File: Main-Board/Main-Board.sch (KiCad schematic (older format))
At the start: 24 parts, among them J1 Power_In, J2 ESC_1, J3 ESC_2, J4 ESC_3, J5 ESC_4, J8 Receiver, J9 Aux, U1 MCP6001U

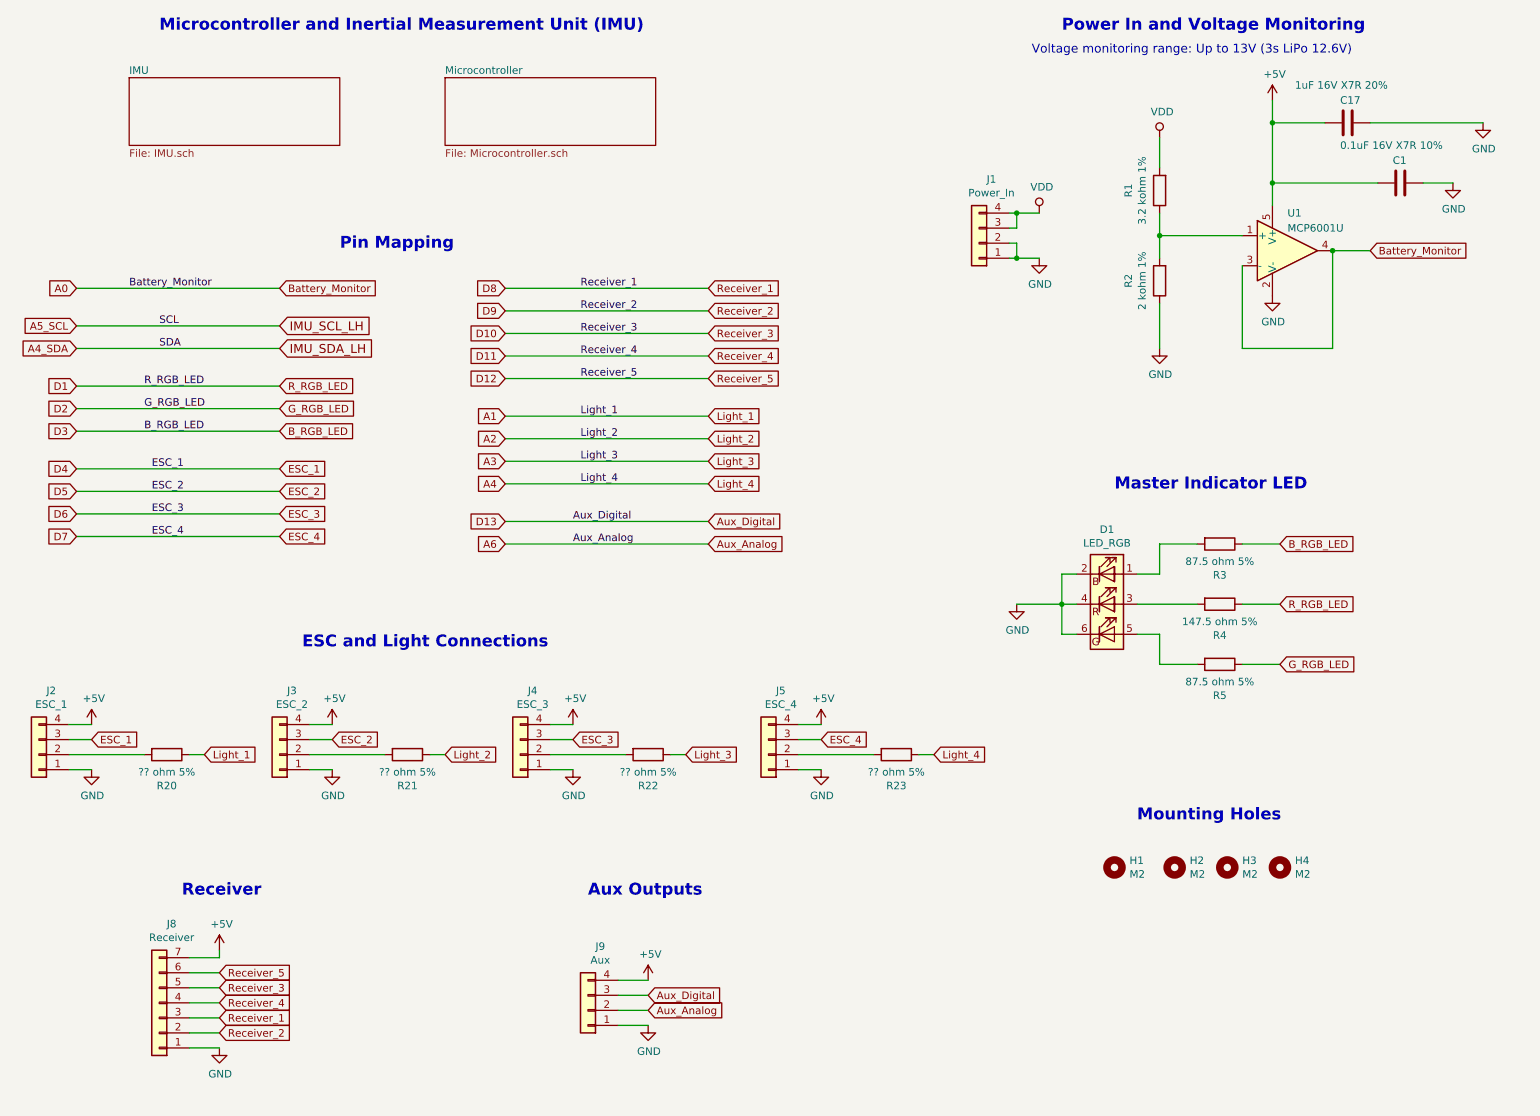
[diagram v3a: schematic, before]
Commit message: Review IMU, changed power in connector to 6 pos to prevent mis mating
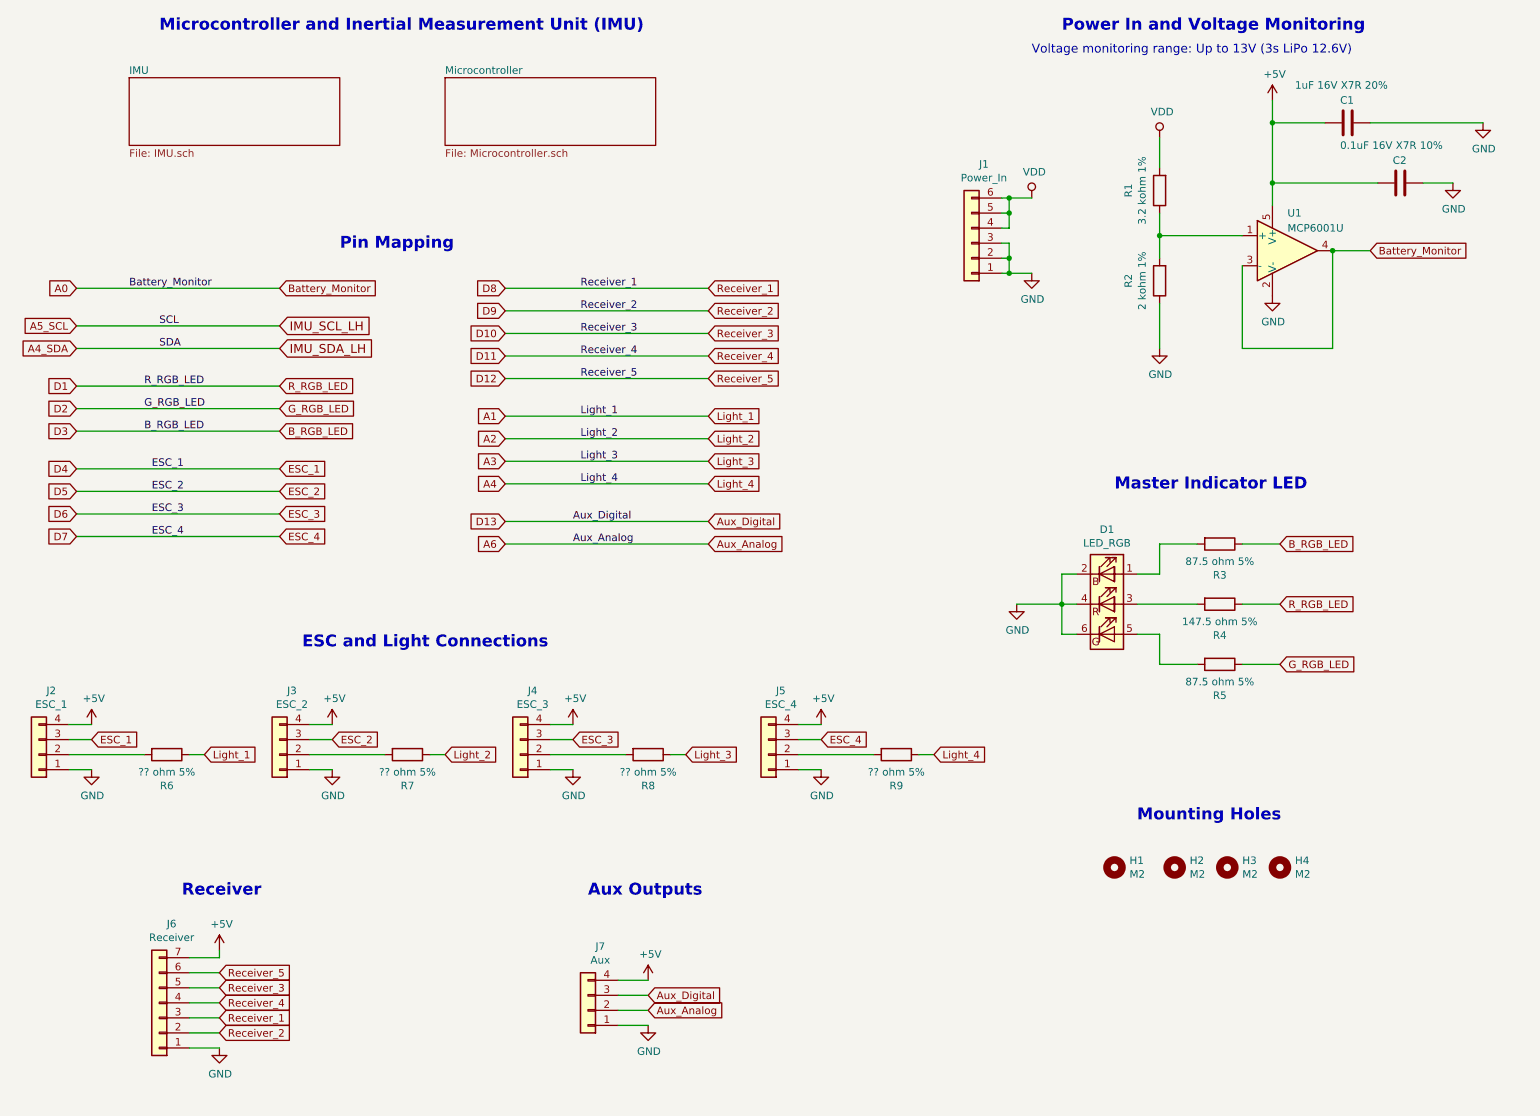
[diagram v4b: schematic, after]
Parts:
- removed J1: Power_In, Connector_JST:JST_GH_BM04B-GHS-TBT_1x04-1MP_P1.25mm_Vertical, symbol Connector_Generic:Conn_01x04
- added J1: Power_In, Connector_JST:JST_GH_BM06B-GHS-TBT_1x06-1MP_P1.25mm_Vertical, symbol Connector_Generic:Conn_01x06
- renumbered C17 to C1, C1 to C2, J8 to J6, J9 to J7, R20 to R6, R21 to R7, R22 to R8, R23 to R9
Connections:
- net GND: now also J1.1 (Pin_1), J1.2 (Pin_2), J1.3 (Pin_3)
- net VDD: now also J1.4 (Pin_4), J1.5 (Pin_5), J1.6 (Pin_6)

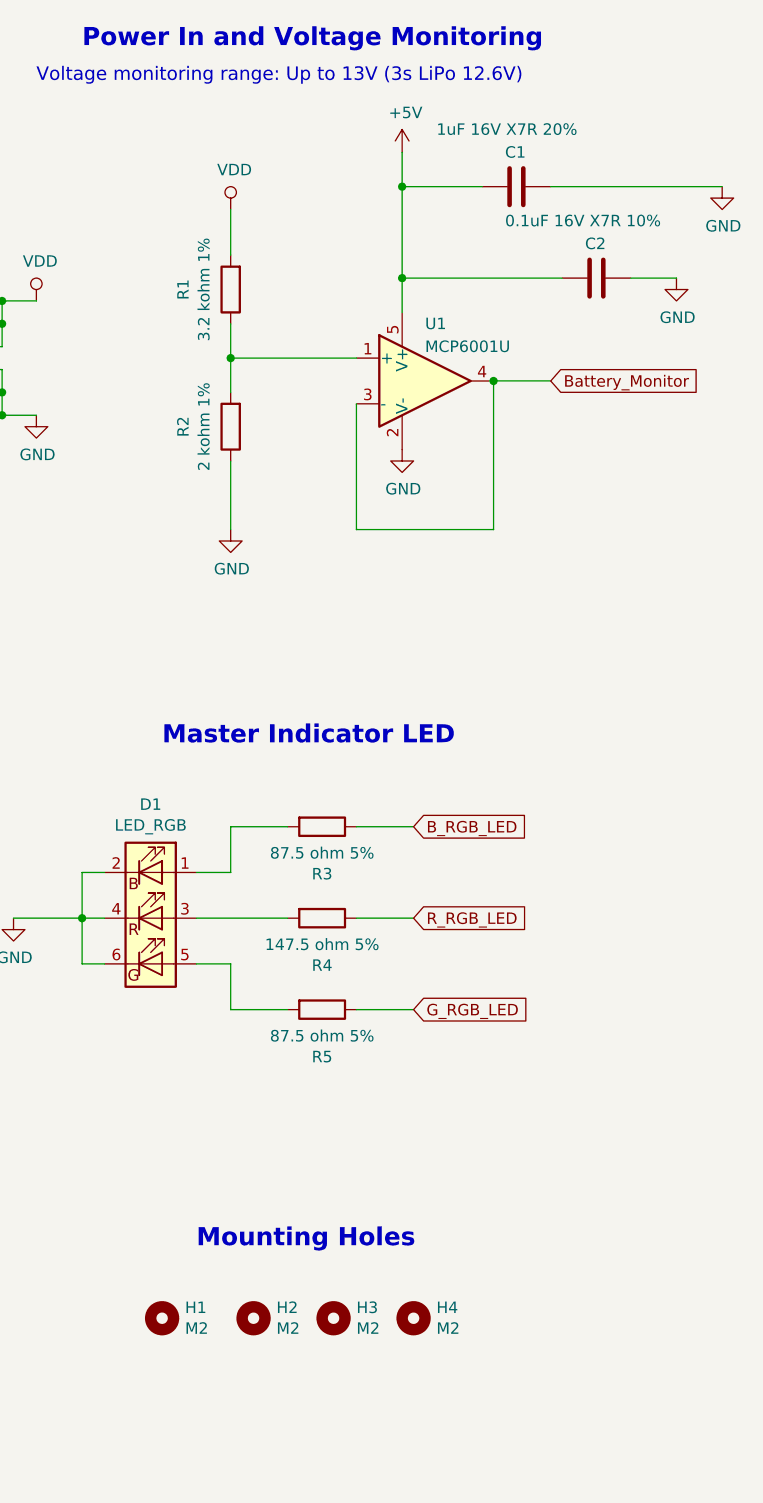
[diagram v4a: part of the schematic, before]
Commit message: Minor updates for components to reflect BOM
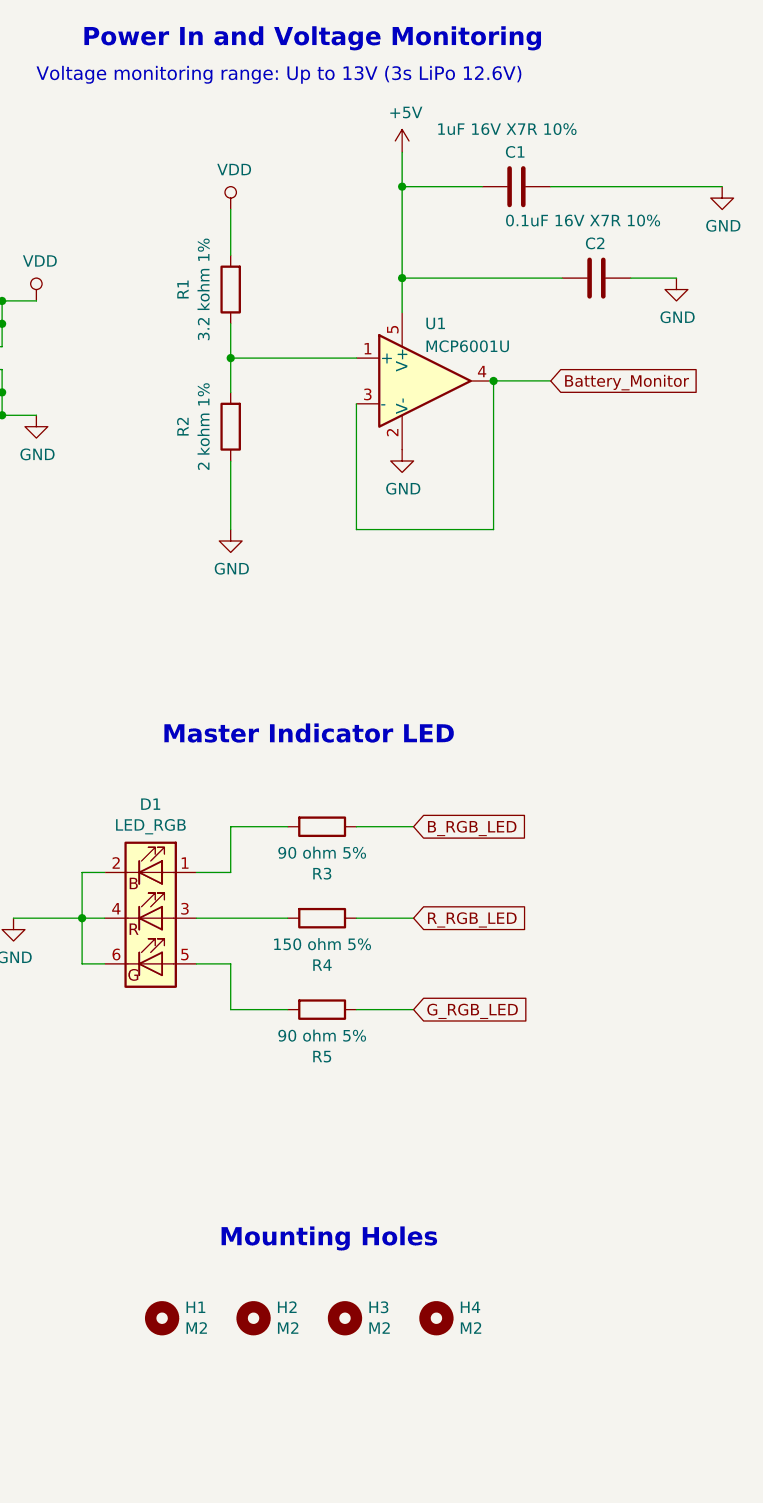
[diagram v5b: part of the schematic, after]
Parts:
- C1: value 1uF 16V X7R 20% -> 1uF 16V X7R 10%
- R3, R5: value 87.5 ohm 5% -> 90 ohm 5%
- R4: value 147.5 ohm 5% -> 150 ohm 5%
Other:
- moved on the sheet: H3, H4
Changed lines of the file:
@@
 encoding utf-8
 Sheet 1 3
-Title "Master Sheet"
-Date "2020-12-19"
+Title "Flight Controller"
+Date "2020-12-21"
 Rev "A"
 Comp ""
@@
 AR Path="/60061C0F" Ref="R3"  Part="1"
 F 0 "R3" V 8807 4150 50  0000 C CNN
-F 1 "87.5 ohm 5%" V 8716 4150 50  0000 C CNN
+F 1 "90 ohm 5%" V 8716 4150 50  0000 C CNN
 F 2 "Resistor_SMD:R_0603_1608Metric_Pad1.05x0.95mm_HandSolder" V 8530 4150 50  0001 C CNN
 F 3 "~" H 8600 4150 50  0001 C CNN
@@
 AR Path="/600625FC" Ref="R4"  Part="1"
 F 0 "R4" V 8807 4550 50  0000 C CNN
-F 1 "147.5 ohm 5%" V 8716 4550 50  0000 C CNN
+F 1 "150 ohm 5%" V 8716 4550 50  0000 C CNN
 F 2 "Resistor_SMD:R_0603_1608Metric_Pad1.05x0.95mm_HandSolder" V 8530 4550 50  0001 C CNN
 F 3 "~" H 8600 4550 50  0001 C CNN
@@
 AR Path="/60062A76" Ref="R5"  Part="1"
 F 0 "R5" V 8807 4950 50  0000 C CNN
-F 1 "87.5 ohm 5%" V 8716 4950 50  0000 C CNN
+F 1 "90 ohm 5%" V 8716 4950 50  0000 C CNN
 F 2 "Resistor_SMD:R_0603_1608Metric_Pad1.05x0.95mm_HandSolder" V 8530 4950 50  0001 C CNN
 F 3 "~" H 8600 4950 50  0001 C CNN
@@
 L Mechanical:MountingHole H3
 U 1 1 5FDEF850
-P 8650 6300
-F 0 "H3" H 8750 6346 50  0000 L CNN
-F 1 "M2" H 8750 6255 50  0000 L CNN
-F 2 "MountingHole:MountingHole_2.2mm_M2_ISO7380_Pad" H 8650 6300 50  0001 C CNN
-F 3 "~" H 8650 6300 50  0001 C CNN
-	1    8650 6300
+P 8700 6300
+F 0 "H3" H 8800 6346 50  0000 L CNN
+F 1 "M2" H 8800 6255 50  0000 L CNN
+F 2 "MountingHole:MountingHole_2.2mm_M2_ISO7380_Pad" H 8700 6300 50  0001 C CNN
+F 3 "~" H 8700 6300 50  0001 C CNN
+	1    8700 6300
 	1    0    0    -1
 $EndComp
@@
 L Mechanical:MountingHole H4
 U 1 1 5FDF1549
-P 9000 6300
-F 0 "H4" H 9100 6346 50  0000 L CNN
-F 1 "M2" H 9100 6255 50  0000 L CNN
-F 2 "MountingHole:MountingHole_2.2mm_M2_ISO7380_Pad" H 9000 6300 50  0001 C CNN
-F 3 "~" H 9000 6300 50  0001 C CNN
-	1    9000 6300
-	1    0    0    -1
-$EndComp
-Text Notes 8050 6000 0    79   ~ 16
+P 9100 6300
+F 0 "H4" H 9200 6346 50  0000 L CNN
+F 1 "M2" H 9200 6255 50  0000 L CNN
+F 2 "MountingHole:MountingHole_2.2mm_M2_ISO7380_Pad" H 9100 6300 50  0001 C CNN
+F 3 "~" H 9100 6300 50  0001 C CNN
+	1    9100 6300
+	1    0    0    -1
+$EndComp
+Text Notes 8150 6000 0    79   ~ 16
 Mounting Holes
 Text Notes 7350 900  0    59   ~ 0
@@
 AR Path="/5FE12F4E" Ref="C1"  Part="1"
 F 0 "C1" V 9600 1300 50  0000 L CNN
-F 1 "1uF 16V X7R 20%" V 9700 1000 50  0000 L CNN
+F 1 "1uF 16V X7R 10%" V 9700 1000 50  0000 L CNN
 F 2 "Capacitor_SMD:C_0603_1608Metric_Pad1.05x0.95mm_HandSolder" H 9488 1200 50  0001 C CNN
 F 3 "~" H 9450 1350 50  0001 C CNN

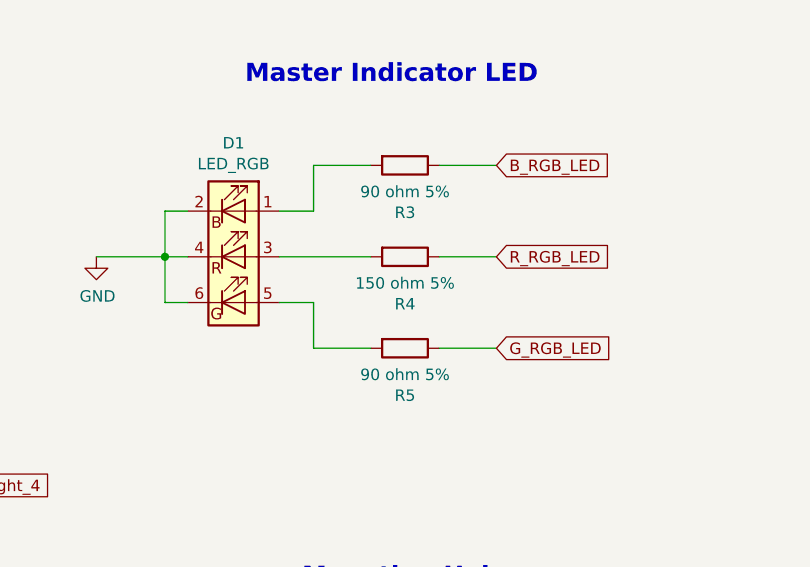
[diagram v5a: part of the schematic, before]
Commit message: Switched from crystal to Resonator
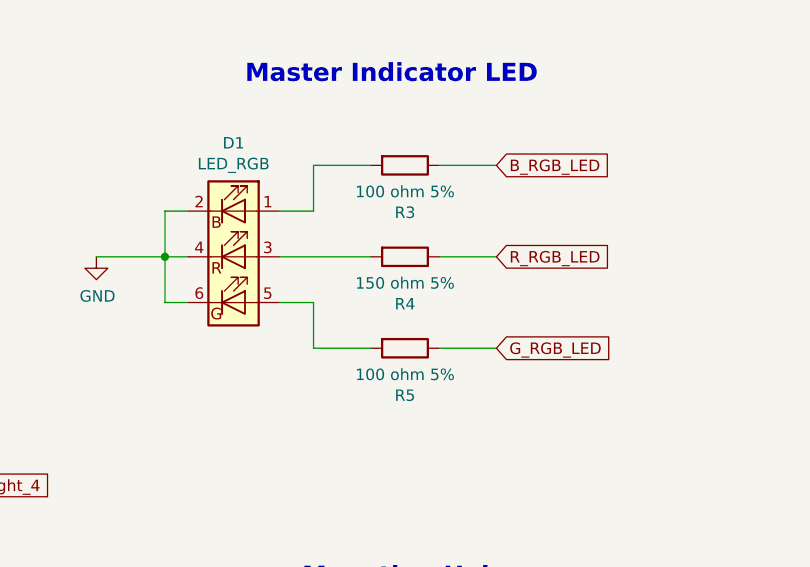
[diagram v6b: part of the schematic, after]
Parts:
- R3, R5: value 90 ohm 5% -> 100 ohm 5%
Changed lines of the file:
@@
 AR Path="/60061C0F" Ref="R3"  Part="1"
 F 0 "R3" V 8807 4150 50  0000 C CNN
-F 1 "90 ohm 5%" V 8716 4150 50  0000 C CNN
+F 1 "100 ohm 5%" V 8716 4150 50  0000 C CNN
 F 2 "Resistor_SMD:R_0603_1608Metric_Pad1.05x0.95mm_HandSolder" V 8530 4150 50  0001 C CNN
 F 3 "~" H 8600 4150 50  0001 C CNN
@@
 AR Path="/60062A76" Ref="R5"  Part="1"
 F 0 "R5" V 8807 4950 50  0000 C CNN
-F 1 "90 ohm 5%" V 8716 4950 50  0000 C CNN
+F 1 "100 ohm 5%" V 8716 4950 50  0000 C CNN
 F 2 "Resistor_SMD:R_0603_1608Metric_Pad1.05x0.95mm_HandSolder" V 8530 4950 50  0001 C CNN
 F 3 "~" H 8600 4950 50  0001 C CNN

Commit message: Shrunk board to approx 65 mm and layed out approx positions
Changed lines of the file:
@@
 ESC and Light Connections
-$Comp
-L Custom:LED_RGB D1
-U 1 1 6009D7CE
-P 7850 4550
-F 0 "D1" H 7850 5047 50  0000 C CNN
-F 1 "LED_RGB" H 7850 4956 50  0000 C CNN
-F 2 "Custom:RGB_LED" H 7850 4500 50  0001 C CNN
-F 3 "~" H 7850 4500 50  0001 C CNN
-F 4 "Everlight Electronics Co Ltd" H 7850 4550 50  0001 C CNN "Manufacturer"
-F 5 "EAST1616RGBA4" H 7850 4550 50  0001 C CNN "Manufacturer #"
-F 6 "1080-EAST1616RGBA4CT-ND" H 7850 4550 50  0001 C CNN "Digi-Key #"
-F 7 "https://www.digikey.ca/en/products/detail/everlight-electronics-co-ltd/EAST1616RGBA4/11200796" H 7850 4550 50  0001 C CNN "Digi-Key LinkDigi LinkDigi-Key Link"
-	1    7850 4550
-	1    0    0    -1
-$EndComp
 $Comp
 L power:GND #PWR09
@@
 	8750 4150 9000 4150
 Wire Wire Line
-	9000 4550 8750 4550
-Wire Wire Line
 	9000 4950 8750 4950
 Wire Wire Line
 	8200 4950 8450 4950
-Wire Wire Line
-	8050 4550 8450 4550
 Text GLabel 1000 3650 0    50   Input ~ 0
 D4
@@
 	7200 2050 7200 1950
 Connection ~ 7200 1950
+$Comp
+L Custom:LED_RGB D1
+U 1 1 6009D7CE
+P 7850 4550
+F 0 "D1" H 7850 5047 50  0000 C CNN
+F 1 "LED_RGB" H 7850 4956 50  0000 C CNN
+F 2 "Custom:RGB_LED" H 7850 4500 50  0001 C CNN
+F 3 "~" H 7850 4500 50  0001 C CNN
+F 4 "Everlight Electronics Co Ltd" H 7850 4550 50  0001 C CNN "Manufacturer"
+F 5 "EAST1616RGBA4" H 7850 4550 50  0001 C CNN "Manufacturer #"
+F 6 "1080-EAST1616RGBA4CT-ND" H 7850 4550 50  0001 C CNN "Digi-Key #"
+F 7 "https://www.digikey.ca/en/products/detail/everlight-electronics-co-ltd/EAST1616RGBA4/11200796" H 7850 4550 50  0001 C CNN "Digi-Key LinkDigi LinkDigi-Key Link"
+	1    7850 4550
+	1    0    0    -1
+$EndComp
+Wire Wire Line
+	8050 4550 8450 4550
+Wire Wire Line
+	8750 4550 9000 4550
 $EndSCHEMATC
